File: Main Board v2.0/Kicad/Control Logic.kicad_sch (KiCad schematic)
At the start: 20 parts, among them J2 +3V3 Supply, J3 JTAG, U7 XC95288XL-TQ144, U8 AP1117-33

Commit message: board rev a routed
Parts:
- renumbered R32 to R35, R33 to R36, R34 to R37
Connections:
- net BC12 is gone; now on net BC13: U7.15 (P15)
- net A10: now also U7.44 (P44); no longer U7.43 (P43)
- net A11: now also U7.45 (P45); no longer U7.44 (P44)
- net A6: now also U7.39 (P39); no longer U7.38 (I/O/GCK3)
- net A7: now also U7.40 (P40); no longer U7.39 (P39)
- net A8: now also U7.41 (P41); no longer U7.40 (P40)
- net A9: now also U7.43 (P43); no longer U7.41 (P41)
- net BC13: no longer U7.14 (P14)
- net BC14: now also U7.14 (P14); no longer U7.13 (P13)
- net BC15: now also U7.13 (P13); no longer U7.12 (P12)
- net BC16: now also U7.12 (P12); no longer U7.11 (P11)
- net BC17: now also U7.11 (P11); no longer U7.10 (P10)
- net BC18: now also U7.10 (P10); no longer U7.9 (P9)
- net BINTACK0: now also U7.92 (P92); no longer U7.118 (P118)
- net D0: now also U7.58 (P58); no longer U7.57 (P57)
- net D1: now also U7.59 (P59); no longer U7.58 (P58)
- net D2: now also U7.60 (P60); no longer U7.59 (P59)
- net D3: now also U7.61 (P61); no longer U7.60 (P60)
- net D4: now also U7.64 (P64); no longer U7.61 (P61)
- net D5: now also U7.66 (P66); no longer U7.64 (P64)
- net D6: now also U7.68 (P68); no longer U7.66 (P66)
- net D7: now also U7.69 (P69); no longer U7.68 (P68)
- net GND: now also U7.38 (I/O/GCK3)
- net MA12: now also U7.46 (P46); no longer U7.45 (P45)
- net MA13: now also U7.48 (P48); no longer U7.46 (P46)
- net MA14: now also U7.49 (P49); no longer U7.48 (P48)
- net MA15: now also U7.50 (P50); no longer U7.49 (P49)
- net MA16: now also U7.51 (P51); no longer U7.50 (P50)
- net MA17: now also U7.52 (P52); no longer U7.51 (P51)
- net MA18: now also U7.53 (P53); no longer U7.52 (P52)
- net MA19: now also U7.54 (P54); no longer U7.53 (P53)
- net MA20: now also U7.56 (P56); no longer U7.54 (P54)
- net MA21: now also U7.57 (P57); no longer U7.56 (P56)
- net MMU_MAP0: now also U7.111 (P111); no longer U7.95 (P95)
- net MMU_MAP1: now also U7.112 (P112); no longer U7.96 (P96)
- net MMU_MAP10: now also U7.117 (P117); no longer U7.107 (P107)
- net MMU_MAP2: now also U7.113 (P113); no longer U7.97 (P97)
- net MMU_MAP3: now also U7.115 (P115); no longer U7.98 (P98)
- net MMU_MAP4: now also U7.107 (P107); no longer U7.100 (P100)
- net MMU_MAP5: now also U7.106 (P106); no longer U7.101 (P101)
- net MMU_MAP6: now also U7.103 (P103); no longer U7.102 (P102)
- net MMU_MAP7: now also U7.104 (P104); no longer U7.103 (P103)
- net MMU_MAP8: now also U7.116 (P116); no longer U7.104 (P104)
- net MMU_MAP9: now also U7.110 (P110); no longer U7.105 (P105)
- net MMU_MP_EXE: now also U7.97 (P97); no longer U7.115 (P115)
- net MMU_MP_RD: now also U7.96 (P96); no longer U7.112 (P112)
- net MMU_MP_WR: now also U7.100 (P100); no longer U7.113 (P113)
- net MMU_RAM_DDIR: now also U7.95 (P95); no longer U7.92 (P92)
- net ~{BIACK}: now also U7.91 (P91); no longer U7.121 (P121)
- net ~{CPU_HALT}: now also U7.129 (P129); no longer U7.119 (P119)
- net ~{CPU_M1}: now also U7.71 (P71); no longer U7.70 (P70)
- net ~{CPU_MREQ}: now also U7.9 (P9); no longer U7.143 (I/O/GSR)
- net ~{CPU_NMI}: now also U7.119 (P119); no longer U7.129 (P129)
- net ~{CPU_RST}: now also U7.143 (I/O/GSR); no longer U7.71 (P71)
- net ~{CPU_WAIT}: now also U7.70 (P70); no longer U7.69 (P69)
- net ~{MMU_RAM1_CE}: now also U7.105 (P105); no longer U7.110 (P110)
- net ~{MMU_RAM1_WE}: now also U7.101 (P101); no longer U7.111 (P111)
- net ~{MMU_RAM2_CE}: now also U7.98 (P98); no longer U7.106 (P106)
- net ~{MMU_RAM2_WE}: now also U7.102 (P102); no longer U7.91 (P91)
- net ~{RAM_CE}: now also U7.118 (P118); no longer U7.116 (P116)
- net ~{ROM_CE}: now also U7.121 (P121); no longer U7.117 (P117)
- net BC11 renamed ~{BBUSRQ}

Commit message: tdo/tdi swap text
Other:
- note added: "Currently using 3x 10k"
- note added: "This is the layout of the Xilinx USB Cable header, as depicted on the case. I should have connected the TDI to the chip's TDO and the TDO to the chip's TDI. You will need to make a cross-cable when connecting the Xilinx programmer to the board."
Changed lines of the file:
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@@
+		)
+	)
+	(text "This is the layout of the Xilinx USB Cable header,\nas depicted on the case.\nI should have connected the TDI to the chip's TDO\nand the TDO to the chip's TDI.\n\nYou will need to make a cross-cable when connecting the\nXilinx programmer to the board."
+		(exclude_from_sim no)
+		(at 71.12 274.828 0)
+		(effects
+			(font
+				(size 1.27 1.27)
+			)
+		)
+	)
+	(text "Currently using 3x 10k"
+		(exclude_from_sim no)
+		(at 114.046 246.126 0)
+		(effects
+			(font
+				(size 1.27 1.27)
+			)
 		)
 	)

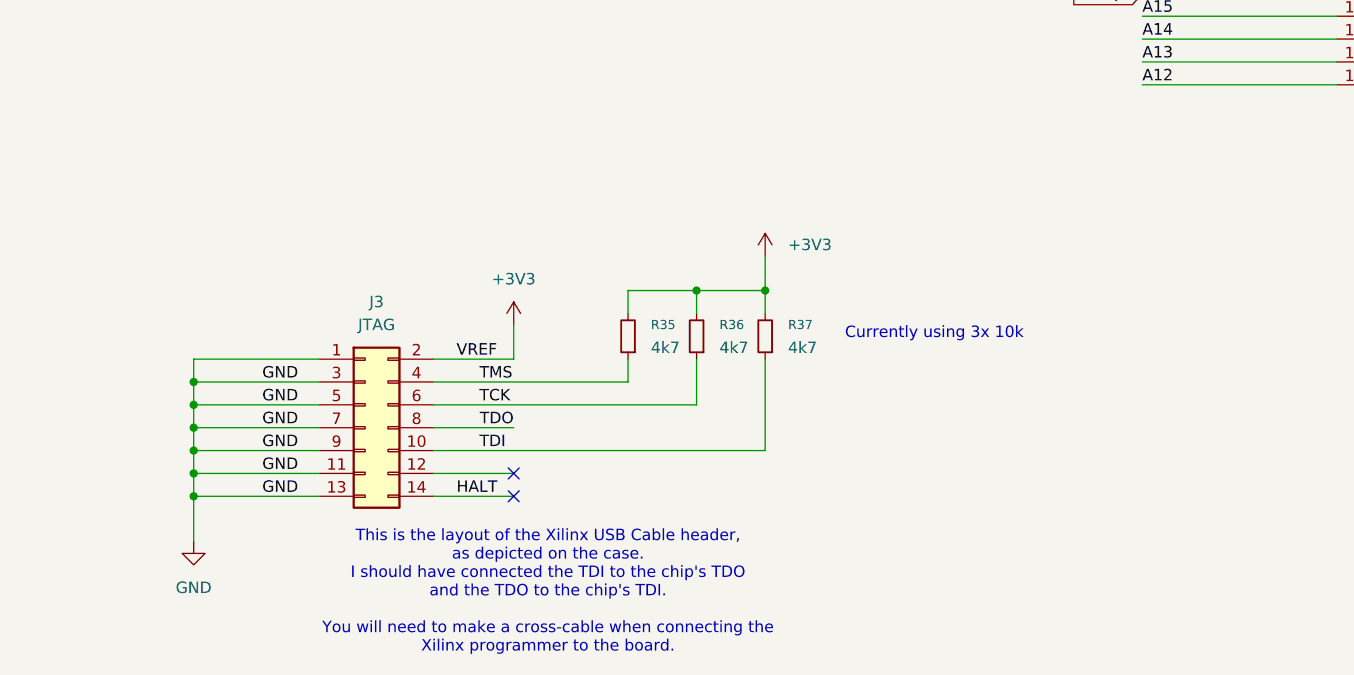
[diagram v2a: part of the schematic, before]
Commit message: update jtag schematic comments
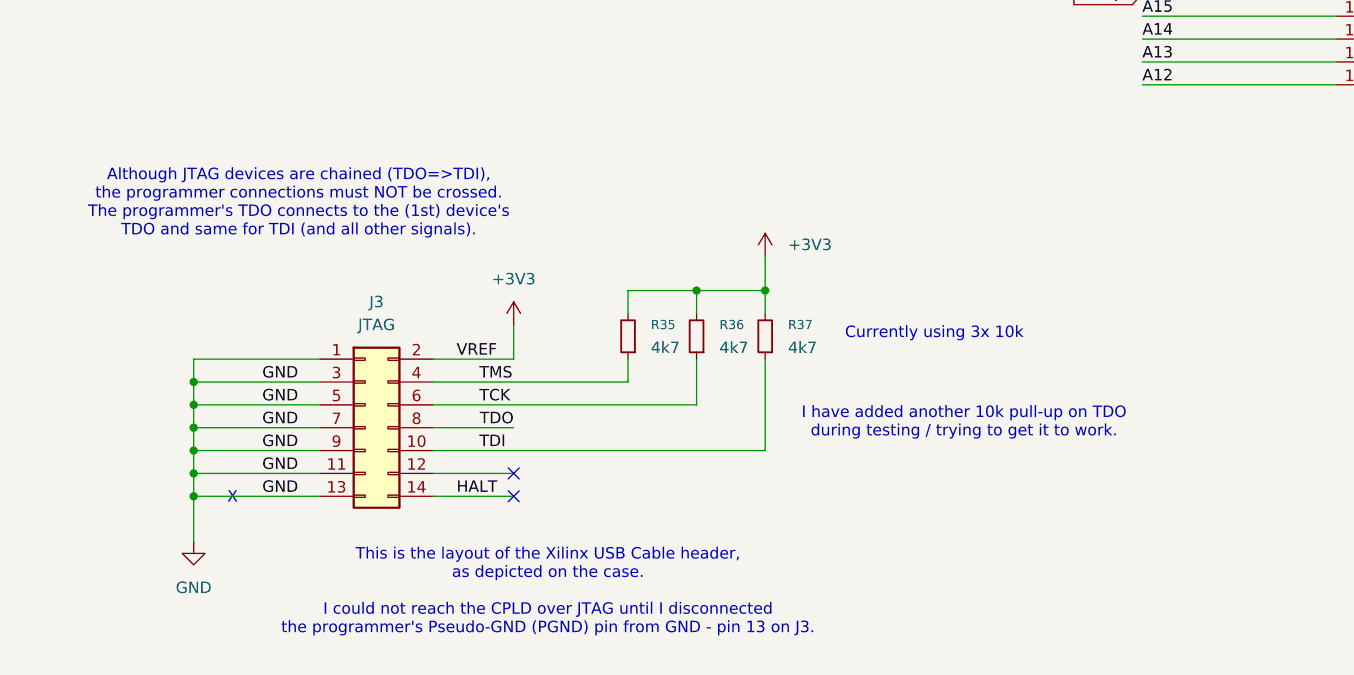
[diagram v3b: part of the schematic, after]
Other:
- note added: "Although JTAG devices are chained (TDO=>TDI), the programmer connections must NOT be crossed. The programmer's TDO connects to the (1st) device's TDO and same for TDI (and all other signals)."
- note added: "I have added another 10k pull-up on TDO during testing / trying to get it to work."
- note added: "This is the layout of the Xilinx USB Cable header, as depicted on the case. I could not reach the CPLD over JTAG until I disconnected the programmer's Pseudo-GND (PGND) pin from GND - pin 13 on J3."
- note added: "X"
- note removed: "This is the layout of the Xilinx USB Cable header, as depicted on the case. I should have connected the TDI to the chip's TDO and the TDO to the chip's TDI. You will need to make a cross-cable when connecting the Xilinx programmer to the board."
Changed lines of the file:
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@@
+		)
+	)
+	(text "I have added another 10k pull-up on TDO\nduring testing / trying to get it to work."
+		(exclude_from_sim no)
+		(at 117.348 256.032 0)
+		(effects
+			(font
+				(size 1.27 1.27)
+			)
+		)
+	)
+	(text "Although JTAG devices are chained (TDO=>TDI),\nthe programmer connections must NOT be crossed.\nThe programmer's TDO connects to the (1st) device's\nTDO and same for TDI (and all other signals)."
+		(exclude_from_sim no)
+		(at 43.434 231.648 0)
+		(effects
+			(font
+				(size 1.27 1.27)
+			)
+		)
+	)
+	(text "X"
+		(exclude_from_sim no)
+		(at 36.068 264.414 0)
+		(effects
+			(font
+				(size 1.27 1.27)
+			)
 		)
 	)
@@
 		)
 	)
-	(text "This is the layout of the Xilinx USB Cable header,\nas depicted on the case.\nI should have connected the TDI to the chip's TDO\nand the TDO to the chip's TDI.\n\nYou will need to make a cross-cable when connecting the\nXilinx programmer to the board."
+	(text "This is the layout of the Xilinx USB Cable header,\nas depicted on the case.\n\nI could not reach the CPLD over JTAG until I disconnected\nthe programmer's Pseudo-GND (PGND) pin from GND - pin 13 on J3."
 		(exclude_from_sim no)
 		(at 71.12 274.828 0)
